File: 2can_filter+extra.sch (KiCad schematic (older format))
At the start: 31 parts, among them J5 54819-0572, J6 NOT_FITTED_SWD_Conn_01x04_Male, U10 74HC4050D, U11 TJA1040T, U12 TJA1040T, U13 TJA1021T, U8 74HC4050D, U9 STM32F105RBTx, Y2 Crystal KX-13 25MHz

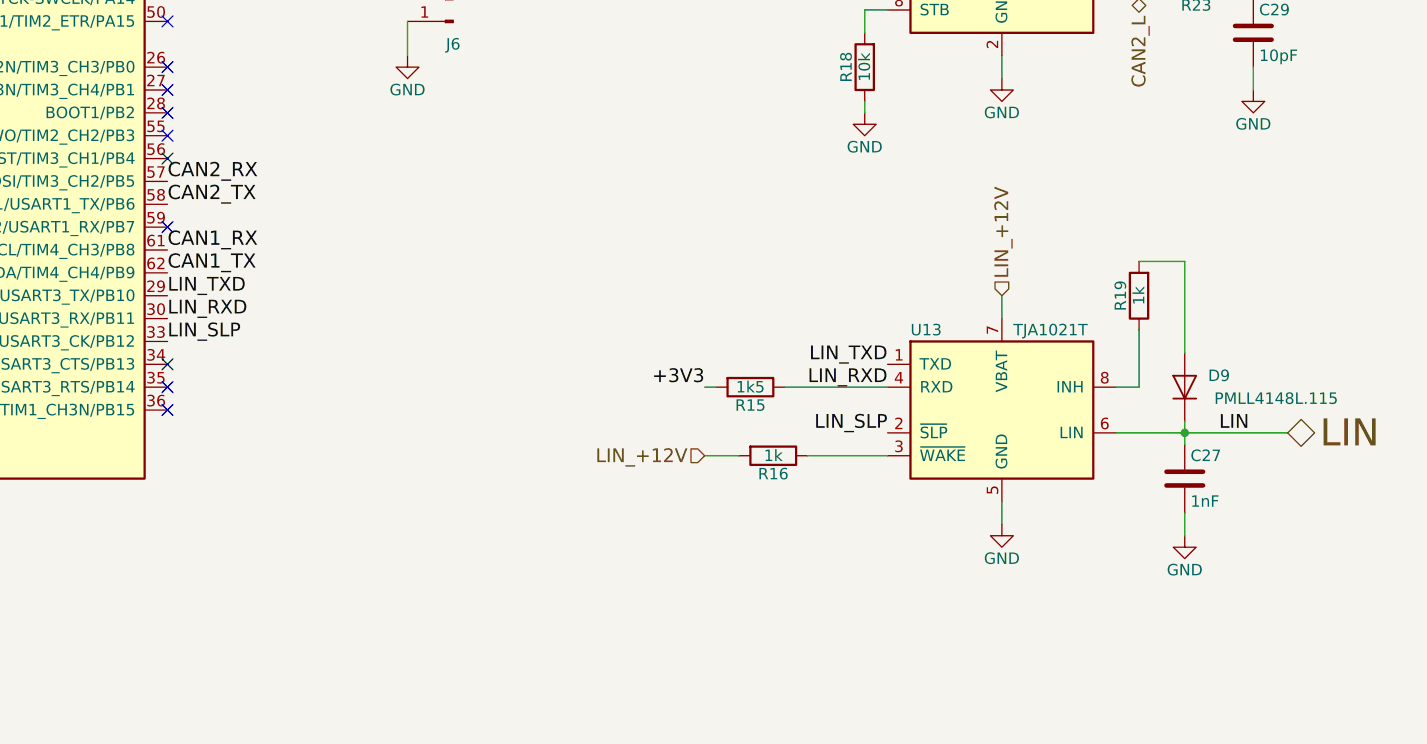
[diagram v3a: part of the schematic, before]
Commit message: delete LIN, fix ERC errors
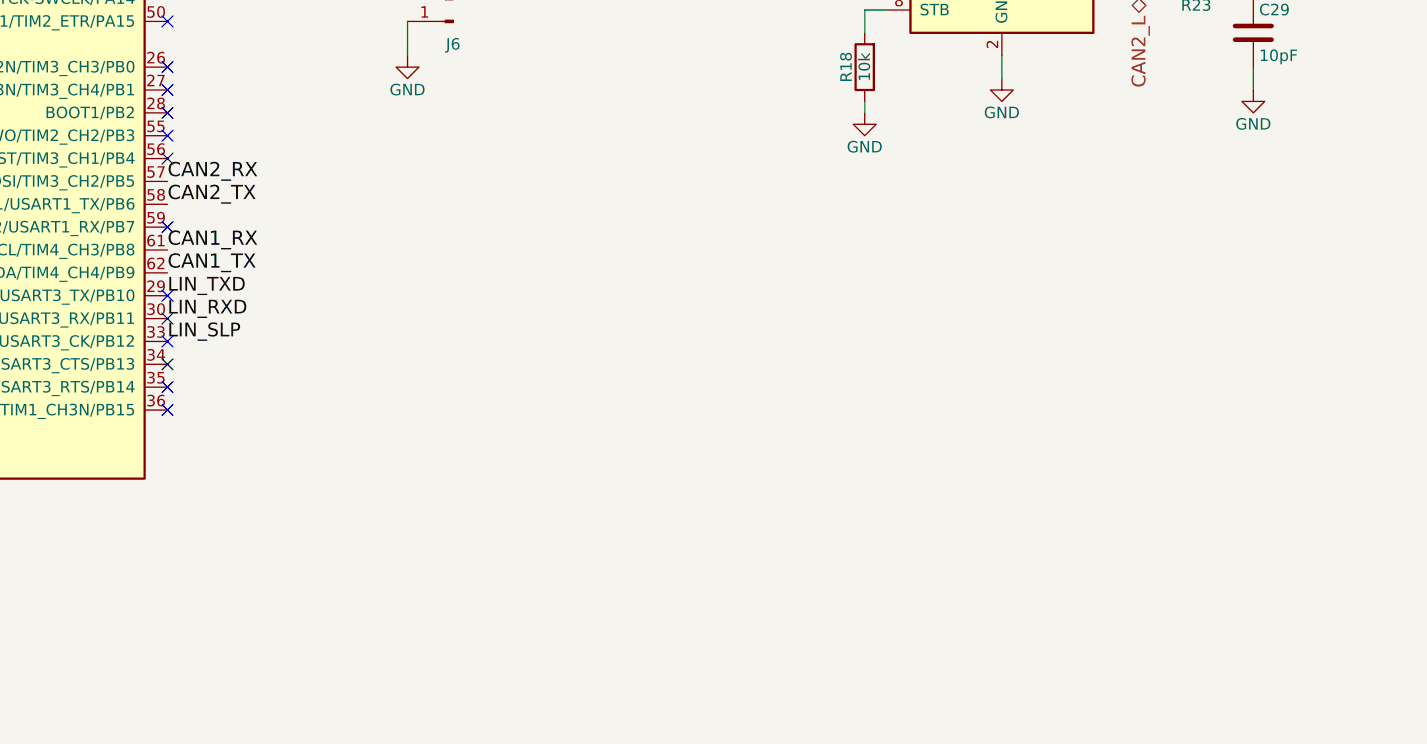
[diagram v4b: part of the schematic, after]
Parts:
- removed C27: 1nF, Capacitors_SMD:C_0805, symbol C
- removed D9: PMLL4148L.115, Diodes_SMD:D_SC-80, symbol D
- removed R15: 1k5, Resistors_SMD:R_0805, symbol R
- removed R16, R19: 1k, Resistors_SMD:R_0805, symbol R
- removed U13: TJA1021T, Housings_SOIC:SOIC-8_3.9x4.9mm_Pitch1.27mm, symbol TJA1021T
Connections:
- no-connect marks 31 -> 34
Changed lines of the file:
@@
 +3V3
 $Comp
-L GND #PWR030
+L GND #PWR031
 U 1 1 5A047DA1
 P 2050 10050
-F 0 "#PWR030" H 2050 9800 50  0001 C CNN
+F 0 "#PWR031" H 2050 9800 50  0001 C CNN
 F 1 "GND" H 2050 9900 50  0000 C CNN
 F 2 "" H 2050 10050 50  0001 C CNN
@@
 Connection ~ 6850 5450
 $Comp
-L GND #PWR031
+L GND #PWR032
 U 1 1 5A0480FC
 P 6950 5550
-F 0 "#PWR031" H 6950 5300 50  0001 C CNN
+F 0 "#PWR032" H 6950 5300 50  0001 C CNN
 F 1 "GND" H 6950 5400 50  0000 C CNN
 F 2 "" H 6950 5550 50  0001 C CNN
@@
 	12800 2200 12800 2250
 $Comp
-L GND #PWR032
+L GND #PWR033
 U 1 1 5A09EB23
 P 13400 2100
-F 0 "#PWR032" H 13400 1850 50  0001 C CNN
+F 0 "#PWR033" H 13400 1850 50  0001 C CNN
 F 1 "GND" H 13400 1950 50  0000 C CNN
 F 2 "" H 13400 2100 50  0001 C CNN
@@
 	13400 2000 13400 2100
 $Comp
-L GND #PWR033
+L GND #PWR034
 U 1 1 5A048D93
 P 14500 2100
-F 0 "#PWR033" H 14500 1850 50  0001 C CNN
+F 0 "#PWR034" H 14500 1850 50  0001 C CNN
 F 1 "GND" H 14500 1950 50  0000 C CNN
 F 2 "" H 14500 2100 50  0001 C CNN
@@
 	14500 2100 14500 2050
 $Comp
-L GND #PWR034
+L GND #PWR035
 U 1 1 5A048E0B
 P 12800 2250
-F 0 "#PWR034" H 12800 2000 50  0001 C CNN
+F 0 "#PWR035" H 12800 2000 50  0001 C CNN
 F 1 "GND" H 12800 2100 50  0000 C CNN
 F 2 "" H 12800 2250 50  0001 C CNN
@@
 	12800 3600 12800 3650
 $Comp
-L GND #PWR035
+L GND #PWR036
 U 1 1 5A048FA0
 P 12800 3650
-F 0 "#PWR035" H 12800 3400 50  0001 C CNN
+F 0 "#PWR036" H 12800 3400 50  0001 C CNN
 F 1 "GND" H 12800 3500 50  0000 C CNN
 F 2 "" H 12800 3650 50  0001 C CNN
@@
 $EndComp
 $Comp
-L GND #PWR036
+L GND #PWR037
 U 1 1 5A049172
 P 13400 3500
-F 0 "#PWR036" H 13400 3250 50  0001 C CNN
+F 0 "#PWR037" H 13400 3250 50  0001 C CNN
 F 1 "GND" H 13400 3350 50  0000 C CNN
 F 2 "" H 13400 3500 50  0001 C CNN
@@
 	13400 3400 13400 3500
 $Comp
-L GND #PWR037
+L GND #PWR038
 U 1 1 5A09EB29
 P 14500 3550
-F 0 "#PWR037" H 14500 3300 50  0001 C CNN
+F 0 "#PWR038" H 14500 3300 50  0001 C CNN
 F 1 "GND" H 14500 3400 50  0000 C CNN
 F 2 "" H 14500 3550 50  0001 C CNN
@@
 	10800 3400 10800 3250
 $Comp
-L GND #PWR038
+L GND #PWR039
 U 1 1 5A09EB2C
 P 10800 3400
-F 0 "#PWR038" H 10800 3150 50  0001 C CNN
+F 0 "#PWR039" H 10800 3150 50  0001 C CNN
 F 1 "GND" H 10800 3250 50  0000 C CNN
 F 2 "" H 10800 3400 50  0001 C CNN
@@
 $EndComp
 $Comp
-L GND #PWR039
+L GND #PWR040
 U 1 1 5A09EB31
 P 2450 4050
-F 0 "#PWR039" H 2450 3800 50  0001 C CNN
+F 0 "#PWR040" H 2450 3800 50  0001 C CNN
 F 1 "GND" H 2450 3900 50  0000 C CNN
 F 2 "" H 2450 4050 50  0001 C CNN
@@
 Connection ~ 2750 3600
 $Comp
-L GND #PWR040
+L GND #PWR041
 U 1 1 5A09EB32
 P 6400 9900
-F 0 "#PWR040" H 6400 9650 50  0001 C CNN
+F 0 "#PWR041" H 6400 9650 50  0001 C CNN
 F 1 "GND" H 6400 9750 50  0000 C CNN
 F 2 "" H 6400 9900 50  0001 C CNN
@@
 Wire Wire Line
 	6400 9750 6400 9900
-$Comp
-L TJA1021T U13
-U 1 1 5A09B465
-P 13400 4950
-F 0 "U13" H 13000 5300 50  0000 L CNN
-F 1 "TJA1021T" H 13450 5300 50  0000 L CNN
-F 2 "Housings_SOIC:SOIC-8_3.9x4.9mm_Pitch1.27mm" H 13400 4450 50  0001 C CIN
-F 3 "" H 13000 5400 50  0001 C CNN
-	1    13400 4950
-	1    0    0    -1
-$EndComp
 Text HLabel 9400 7300 0    60   Input ~ 0
 TRIP_COMPUTER
@@
 Connection ~ 9950 10300
 $Comp
-L GND #PWR041
+L GND #PWR042
 U 1 1 5A09F076
 P 10400 10600
-F 0 "#PWR041" H 10400 10350 50  0001 C CNN
+F 0 "#PWR042" H 10400 10350 50  0001 C CNN
 F 1 "GND" H 10400 10450 50  0000 C CNN
 F 2 "" H 10400 10600 50  0001 C CNN
@@
 anti-theft
 $Comp
-L GND #PWR042
+L GND #PWR043
 U 1 1 5A0A1F34
 P 6300 7850
-F 0 "#PWR042" H 6300 7600 50  0001 C CNN
+F 0 "#PWR043" H 6300 7600 50  0001 C CNN
 F 1 "GND" H 6300 7700 50  0000 C CNN
 F 2 "" H 6300 7850 50  0001 C CNN
@@
 NoConn ~ 9750 4850
 NoConn ~ 9750 4950
-$Comp
-L R R19
-U 1 1 5A0B8C74
-P 14000 4450
-F 0 "R19" V 14080 4450 50  0000 C CNN
-F 1 "1k" V 14000 4450 50  0000 C CNN
-F 2 "Resistors_SMD:R_0805" V 13930 4450 50  0001 C CNN
-F 3 "" H 14000 4450 50  0001 C CNN
-	1    14000 4450
-	-1   0    0    1
-$EndComp
-$Comp
-L R R15
-U 1 1 5A0B8CED
-P 12300 4850
-F 0 "R15" V 12380 4850 50  0000 C CNN
-F 1 "1k5" V 12300 4850 50  0000 C CNN
-F 2 "Resistors_SMD:R_0805" V 12230 4850 50  0001 C CNN
-F 3 "" H 12300 4850 50  0001 C CNN
-	1    12300 4850
-	0    1    1    0
-$EndComp
-$Comp
-L R R16
-U 1 1 5A0B8DE4
-P 12400 5150
-F 0 "R16" V 12480 5150 50  0000 C CNN
-F 1 "1k" V 12400 5150 50  0000 C CNN
-F 2 "Resistors_SMD:R_0805" V 12330 5150 50  0001 C CNN
-F 3 "" H 12400 5150 50  0001 C CNN
-	1    12400 5150
-	0    1    1    0
-$EndComp
-$Comp
-L C C27
-U 1 1 5A0B8E49
-P 14200 5250
-F 0 "C27" H 14225 5350 50  0000 L CNN
-F 1 "1nF" H 14225 5150 50  0000 L CNN
-F 2 "Capacitors_SMD:C_0805" H 14238 5100 50  0001 C CNN
-F 3 "" H 14200 5250 50  0001 C CNN
-	1    14200 5250
-	1    0    0    -1
-$EndComp
-Text Label 12900 4850 2    60   ~ 0
-LIN_RXD
-Text Label 12900 4750 2    60   ~ 0
-LIN_TXD
-$Comp
-L D D9
-U 1 1 5A0B90B6
-P 14200 4850
-F 0 "D9" V 14250 4700 50  0000 C CNN
-F 1 "PMLL4148L.115" V 14150 4450 50  0000 C CNN
-F 2 "Diodes_SMD:D_SC-80" H 14200 4850 50  0001 C CNN
-F 3 "" H 14200 4850 50  0001 C CNN
-	1    14200 4850
-	0    -1   -1   0
-$EndComp
-Text HLabel 13400 4450 1    60   Input ~ 0
-LIN_+12V
-Wire Wire Line
-	13400 4450 13400 4550
 Text Label 9750 4450 0    60   ~ 0
 LIN_TXD
 Text Label 9750 4550 0    60   ~ 0
 LIN_RXD
-Wire Wire Line
-	13900 5050 14650 5050
-Wire Wire Line
-	14200 5000 14200 5100
-Connection ~ 14200 5050
-$Comp
-L GND #PWR043
-U 1 1 5A0BEC86
-P 13400 5450
-F 0 "#PWR043" H 13400 5200 50  0001 C CNN
-F 1 "GND" H 13400 5300 50  0000 C CNN
-F 2 "" H 13400 5450 50  0001 C CNN
-F 3 "" H 13400 5450 50  0001 C CNN
-	1    13400 5450
-	1    0    0    -1
-$EndComp
-$Comp
-L GND #PWR044
-U 1 1 5A0BECD4
-P 14200 5500
-F 0 "#PWR044" H 14200 5250 50  0001 C CNN
-F 1 "GND" H 14200 5350 50  0000 C CNN
-F 2 "" H 14200 5500 50  0001 C CNN
-F 3 "" H 14200 5500 50  0001 C CNN
-	1    14200 5500
-	1    0    0    -1
-$EndComp
-Wire Wire Line
-	14200 5400 14200 5500
-Wire Wire Line
-	13400 5350 13400 5450
-Wire Wire Line
-	14200 4700 14200 4300
-Wire Wire Line
-	14200 4300 14000 4300
-Wire Wire Line
-	14000 4600 14000 4850
-Wire Wire Line
-	14000 4850 13900 4850
 Text Label 9750 4650 0    60   ~ 0
 LIN_SLP
-Text Label 12900 5050 2    60   ~ 0
-LIN_SLP
-Wire Wire Line
-	12450 4850 12900 4850
-Wire Wire Line
-	12150 4850 12100 4850
-Wire Wire Line
-	12900 5150 12550 5150
-Wire Wire Line
-	12250 5150 12100 5150
-Text HLabel 12100 5150 0    60   Input ~ 0
-LIN_+12V
-Text Label 12100 4850 2    60   ~ 0
-+3V3
-Text HLabel 14650 5050 2    118  BiDi ~ 0
-LIN
-Text Label 14350 5050 0    60   ~ 0
-LIN
 $Comp
 L R R10
@@
 Connection ~ 6400 9850
 $Comp
-L GND #PWR045
+L GND #PWR044
 U 1 1 5A0EC5D8
 P 9300 7950
-F 0 "#PWR045" H 9300 7700 50  0001 C CNN
+F 0 "#PWR044" H 9300 7700 50  0001 C CNN
 F 1 "GND" H 9300 7800 50  0000 C CNN
 F 2 "" H 9300 7950 50  0001 C CNN
@@
 Wire Wire Line
 	9300 7800 9400 7800
+NoConn ~ 9750 4650
+NoConn ~ 9750 4550
+NoConn ~ 9750 4450
 $EndSCHEMATC

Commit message: add footprints to SWD connectors
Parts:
- J6: footprint (none) -> Pin_Headers:Pin_Header_Straight_1x04_Pitch2.54mm
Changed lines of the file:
@@
 F 0 "J6" H 11000 3350 50  0000 C CNN
 F 1 "NOT_FITTED_SWD_Conn_01x04_Male" H 10800 2750 50  0000 C CNN
-F 2 "" H 11000 3150 50  0001 C CNN
+F 2 "Pin_Headers:Pin_Header_Straight_1x04_Pitch2.54mm" H 11000 3150 50  0001 C CNN
 F 3 "" H 11000 3150 50  0001 C CNN
 	1    11000 3150

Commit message: change usb fp
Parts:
- J5: footprint 54819-0572:MOLEXMINIBTYPEB_1 -> zulljon:USB_mini_B
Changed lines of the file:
@@
 F 0 "J5" H 5800 9800 50  0000 C CNN
 F 1 "54819-0572" H 5800 9300 50  0000 C CNN
-F 2 "54819-0572:MOLEXMINIBTYPEB_1" H 5800 9200 50  0001 C CNN
+F 2 "zulljon:USB_mini_B" H 5800 9200 50  0001 C CNN
 F 3 "http://www.molex.com/webdocs/datasheets/pdf/en-us/0548190572_IO_CONNECTORS.pdf" H 5800 9100 50  0001 C CNN
 F 4 "Surface mount onthego connector,1A 30V Molex On-The-Go Series Right Angle SMT Version 2.0 Type B Mini USB Connector Receptacle, 30 V, 1A" H 5800 9000 50  0001 C CNN "Description"
@@
 F 8 "54819-0572" H 5800 8600 50  0001 C CNN "Manufacturer_Part_Number"
 F 9 "70266924" H 5800 8500 50  0001 C CNN "Allied_Number"
-F 10 "" H 5800 8400 50  0001 C CNN "Other Part Number"
-F 11 "" H 6000 8300 50  0001 C CNN "Height"
 	1    5450 9650
 	1    0    0    -1

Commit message: rescue the stm32 mcu_s, add pcb list info
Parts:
- U9: symbol STM32F105RBTx -> STM32F105RBTx-RESCUE-instrument_cluster
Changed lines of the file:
@@
 EESchema Schematic File Version 2
+LIBS:instrument_cluster-rescue
 LIBS:power
 LIBS:device
@@
 $EndDescr
 $Comp
-L STM32F105RBTx U9
+L STM32F105RBTx-RESCUE-instrument_cluster U9
 U 1 1 5A047502
 P 6950 3350
+AR Path="/5A047502" Ref="U9"  Part="1"
+AR Path="/5A0472F5/5A047502" Ref="U9"  Part="1"
 F 0 "U9" H 4250 5275 50  0000 L BNN
 F 1 "STM32F105RBTx" H 9650 5275 50  0000 R BNN

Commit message: fix labels in fuel_adc
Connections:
- net fuel_adc_1 renamed stm_adc_1
- net fuel_adc_2 renamed stm_adc_2
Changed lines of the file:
@@
 $EndComp
 Wire Wire Line
-	13900 1500 14100 1500
+	13900 1500 14000 1500
+Wire Wire Line
+	14000 1500 14100 1500
 Wire Wire Line
 	14000 1450 14000 1500
@@
 $EndComp
 Wire Wire Line
-	4050 1250 7250 1250
+	4050 1250 6750 1250
+Wire Wire Line
+	6750 1250 6850 1250
+Wire Wire Line
+	6850 1250 6950 1250
+Wire Wire Line
+	6950 1250 7050 1250
+Wire Wire Line
+	7050 1250 7150 1250
+Wire Wire Line
+	7150 1250 7250 1250
 Wire Wire Line
 	7150 1250 7150 1350
@@
 	6750 5350 6750 5450
 Wire Wire Line
-	6750 5450 7150 5450
+	6750 5450 6850 5450
+Wire Wire Line
+	6850 5450 6950 5450
+Wire Wire Line
+	6950 5450 7050 5450
+Wire Wire Line
+	7050 5450 7150 5450
 Wire Wire Line
 	7150 5450 7150 5350
@@
 Connection ~ 7050 5450
 Wire Wire Line
-	6950 5350 6950 5550
+	6950 5350 6950 5450
+Wire Wire Line
+	6950 5450 6950 5550
 Connection ~ 6950 5450
 Wire Wire Line
@@
 +3V3
 Wire Wire Line
-	13900 1700 14100 1700
+	13900 1700 14000 1700
+Wire Wire Line
+	14000 1700 14100 1700
 Wire Wire Line
 	14000 1750 14000 1700
@@
 	13900 1600 14500 1600
 Wire Wire Line
-	14500 1500 14500 1750
+	14500 1500 14500 1600
+Wire Wire Line
+	14500 1600 14500 1700
+Wire Wire Line
+	14500 1700 14500 1750
 Wire Wire Line
 	14500 1700 14400 1700
@@
 	13900 3000 14500 3000
 Wire Wire Line
-	14500 2900 14500 3150
+	14500 2900 14500 3000
+Wire Wire Line
+	14500 3000 14500 3100
+Wire Wire Line
+	14500 3100 14500 3150
 Wire Wire Line
 	14500 3100 14400 3100
@@
 Connection ~ 14500 3000
 Wire Wire Line
-	13900 2900 14100 2900
+	13900 2900 14000 2900
+Wire Wire Line
+	14000 2900 14100 2900
 Wire Wire Line
 	14000 2850 14000 2900
 Connection ~ 14000 2900
 Wire Wire Line
-	13900 3100 14100 3100
+	13900 3100 14000 3100
+Wire Wire Line
+	14000 3100 14100 3100
 Wire Wire Line
 	14000 3150 14000 3100
@@
 SWD_+3V3
 Wire Wire Line
-	2550 9950 3150 9950
+	2550 9950 2900 9950
+Wire Wire Line
+	2900 9950 3150 9950
 Wire Wire Line
 	2900 9750 2900 9950
@@
 	2750 4050 2750 4000
 Wire Wire Line
-	2150 3050 2150 3700
+	2150 3050 2150 3600
+Wire Wire Line
+	2150 3600 2150 3700
 Wire Wire Line
 	2150 3600 2300 3600
@@
 	2600 3600 2750 3600
 Wire Wire Line
-	2750 3150 2750 3700
+	2750 3150 2750 3600
+Wire Wire Line
+	2750 3600 2750 3700
 Connection ~ 2150 3600
 Connection ~ 2750 3600
@@
 	6300 9750 6400 9750
 Wire Wire Line
-	6400 9750 6400 9900
+	6400 9750 6400 9850
+Wire Wire Line
+	6400 9850 6400 9900
 Text HLabel 9400 7300 0    60   Input ~ 0
 TRIP_COMPUTER
@@
 $EndComp
 Wire Wire Line
-	9850 9900 10050 9900
+	9850 9900 9950 9900
+Wire Wire Line
+	9950 9900 10050 9900
 Wire Wire Line
 	9550 9900 9450 9900
@@
 	10350 9900 10400 9900
 Wire Wire Line
-	9950 9900 9950 10100
-Wire Wire Line
-	9950 10100 10500 10100
+	9950 9900 9950 9700
+Wire Wire Line
+	9950 9700 10500 9700
 Connection ~ 9950 9900
 $Comp
@@
 $EndComp
 Wire Wire Line
-	9850 10300 10050 10300
+	9850 10300 9950 10300
+Wire Wire Line
+	9950 10300 10050 10300
 Wire Wire Line
 	9550 10300 9450 10300
@@
 	10350 10300 10400 10300
 Wire Wire Line
-	9950 10300 9950 10500
-Wire Wire Line
-	9950 10500 10500 10500
+	9950 10300 9950 10550
+Wire Wire Line
+	9950 10550 9650 10550
 Connection ~ 9950 10300
 $Comp
@@
 $EndComp
 Wire Wire Line
-	10400 9900 10400 10600
+	10400 9900 10400 10300
+Wire Wire Line
+	10400 10300 10400 10600
 Connection ~ 10400 10300
-Text Label 10500 10100 0    60   ~ 0
-fuel_adc_1
-Text Label 10500 10500 0    60   ~ 0
-fuel_adc_2
-Text Label 9750 1850 0    60   ~ 0
-fuel_adc_1
+Text Label 10500 9700 0    60   ~ 0
+stm_adc_1
+Text Label 9650 10550 2    60   ~ 0
+stm_adc_2
 Wire Wire Line
 	4150 3050 2150 3050
 Wire Wire Line
 	2750 3150 4150 3150
-Text Label 4150 3750 2    60   ~ 0
-fuel_adc_2
 NoConn ~ 10400 7300
 NoConn ~ 10400 7200
@@
 	2450 4050 2450 3800
 Wire Wire Line
-	1900 4050 2750 4050
+	1900 4050 2150 4050
+Wire Wire Line
+	2150 4050 2450 4050
+Wire Wire Line
+	2450 4050 2750 4050
 Connection ~ 2450 4050
 Wire Wire Line
@@
 NoConn ~ 9750 4550
 NoConn ~ 9750 4450
+Text Label 9750 1850 0    60   ~ 0
+stm_adc_1
+Text Label 4150 3750 2    60   ~ 0
+stm_adc_2
 $EndSCHEMATC
